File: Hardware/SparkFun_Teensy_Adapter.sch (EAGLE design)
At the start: 19 parts, among them U1 5V

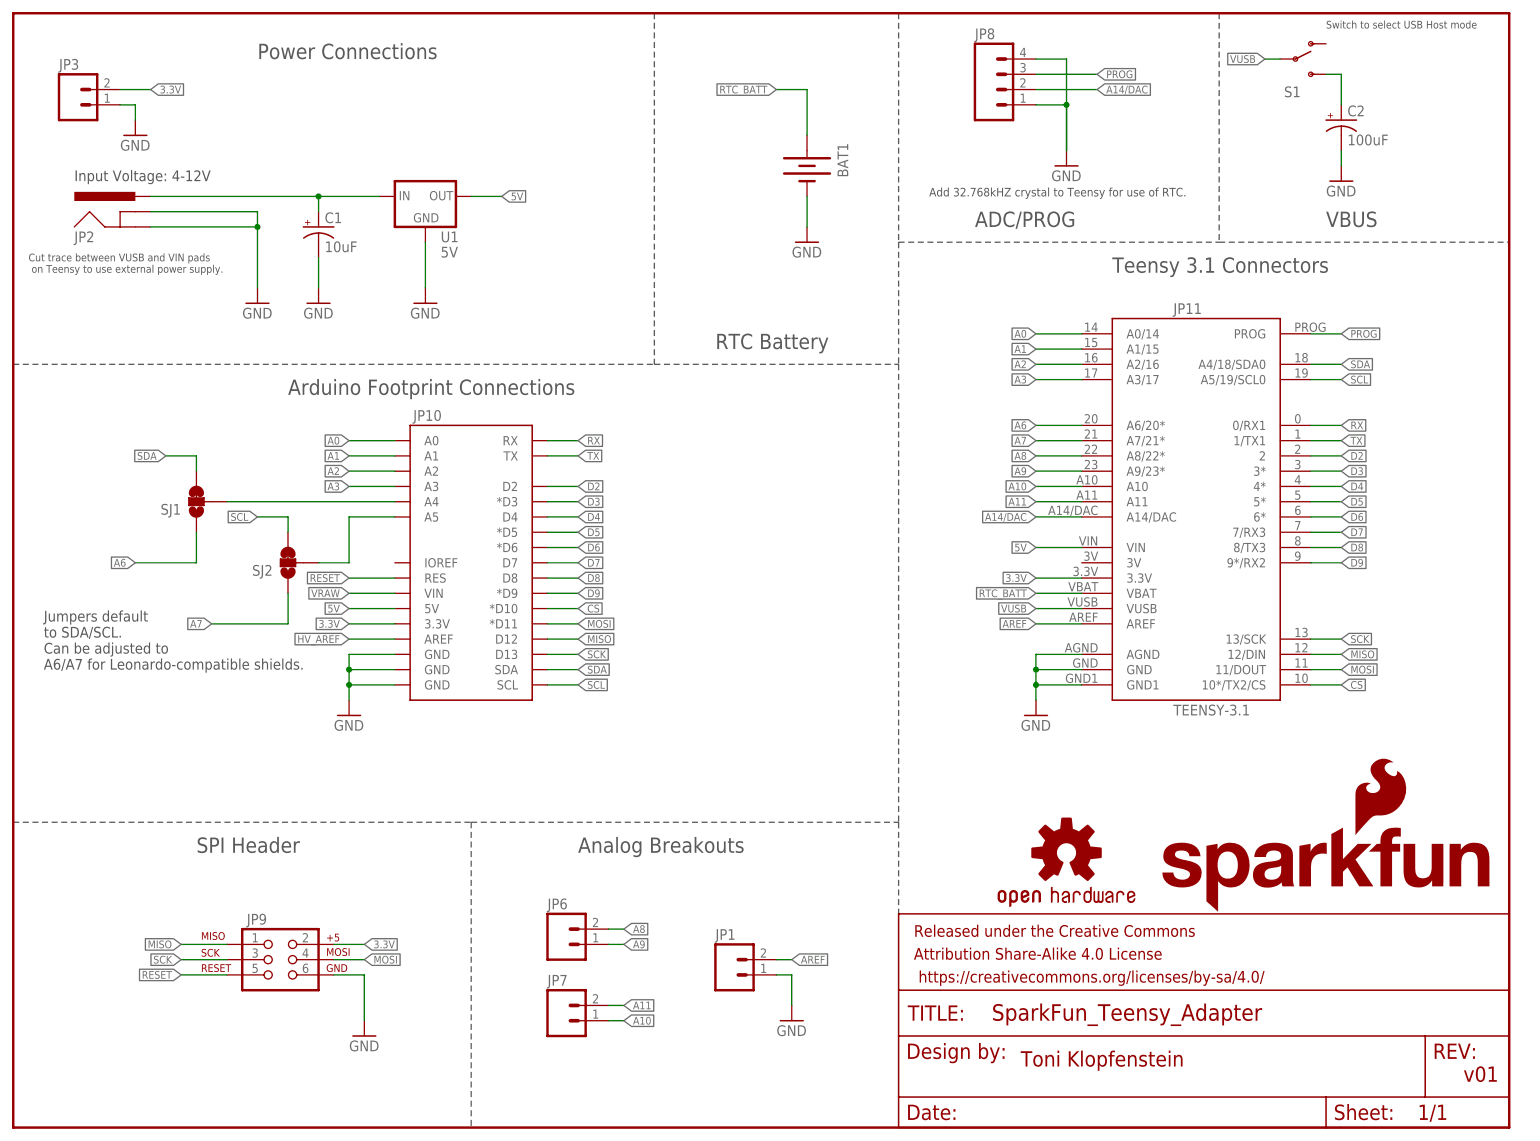
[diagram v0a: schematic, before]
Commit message: Moving vias from under regulator, removing USB host shield parts
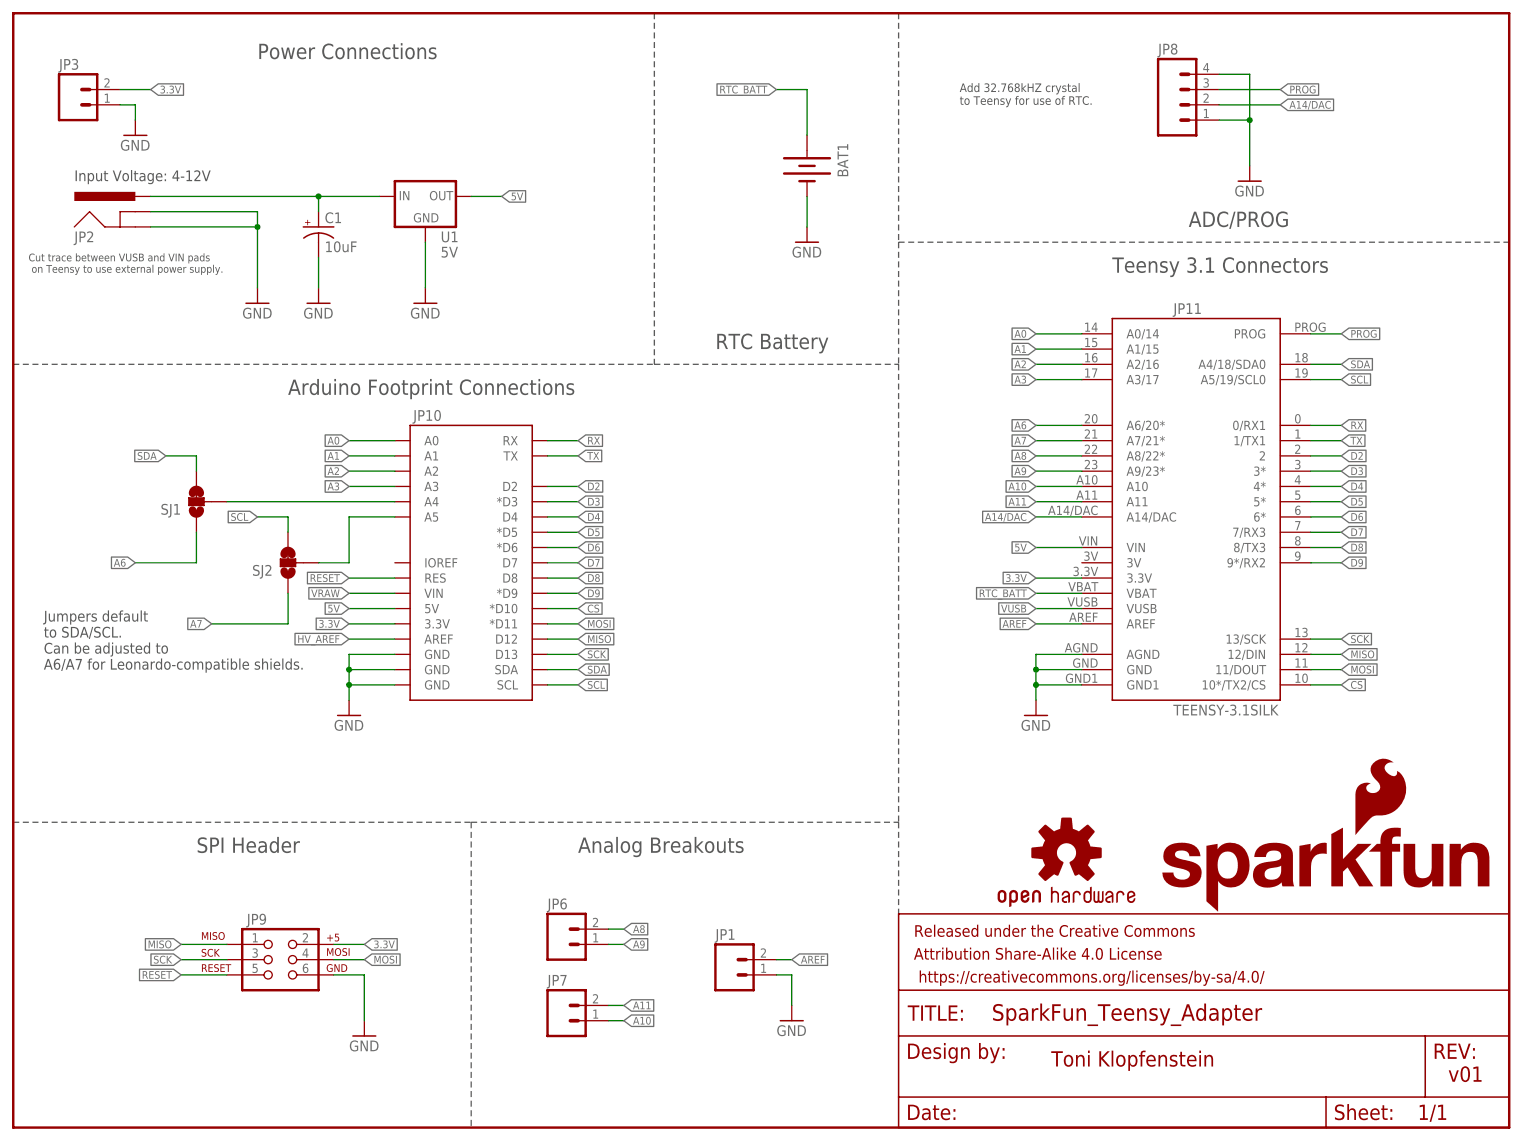
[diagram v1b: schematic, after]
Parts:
- removed C2: 100uF, SparkFun-Capacitors:100UF-25V-20%(PTH)
- removed S1: (no value), SparkFun-Electromechanical:SWITCH-SPDTPTH
- JP1, JP6, JP7: value M02PTH -> (none)
- JP11: value TEENSY-3.1 -> TEENSY-3.1SILK; device Testing:TEENSY-3.1 -> Testing:TEENSY-3.1SILK
- JP3: value M02JST-PTH-2 -> (none)
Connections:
- removed net N$1: C2.+, S1.S
- net GND: no longer C2.-
- net VUSB: no longer S1.P
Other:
- note removed: "Switch to select USB Host mode"
- note removed: "VBUS"
- moved on the sheet: JP8
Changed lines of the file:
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@@
 <layer number="56" name="wert" color="7" fill="1" visible="no" active="no"/>
 <layer number="57" name="tCAD" color="7" fill="1" visible="no" active="no"/>
+<layer number="59" name="tCarbon" color="7" fill="1" visible="no" active="no"/>
+<layer number="60" name="bCarbon" color="7" fill="1" visible="no" active="no"/>
 <layer number="90" name="Modules" color="5" fill="1" visible="yes" active="yes"/>
 <layer number="91" name="Nets" color="2" fill="1" visible="yes" active="yes"/>
@@
 <layer number="127" name="_tValues" color="7" fill="1" visible="yes" active="yes"/>
 <layer number="128" name="_bValues" color="7" fill="1" visible="yes" active="yes"/>
+<layer number="129" name="Mask" color="7" fill="1" visible="yes" active="yes"/>
 <layer number="131" name="tAdjust" color="7" fill="1" visible="yes" active="yes"/>
 <layer number="132" name="bAdjust" color="7" fill="1" visible="yes" active="yes"/>
@@
 <part name="JP10" library="Testing" deviceset="ARDUINO_R3_SHIELD" device="UNO_R3_SHIELD_HOLES"/>
 <part name="JP9" library="SparkFun-Connectors" deviceset="AVR_SPI_PRG_6" device="PTH"/>
-<part name="JP11" library="Testing" deviceset="TEENSY-3.1" device=""/>
+<part name="JP11" library="Testing" deviceset="TEENSY-3.1" device="SILK"/>
 <part name="GND1" library="SparkFun-Aesthetics" deviceset="GND" device=""/>
 <part name="GND2" library="SparkFun-Aesthetics" deviceset="GND" device=""/>
@@
 <part name="JP8" library="SparkFun-Connectors" deviceset="M04" device="PTH"/>
 <part name="GND9" library="SparkFun-Aesthetics" deviceset="GND" device=""/>
-<part name="GND11" library="SparkFun-Aesthetics" deviceset="GND" device=""/>
 <part name="BAT1" library="SparkFun-Electromechanical" deviceset="BATTERY" device="12PTH"/>
 <part name="GND4" library="SparkFun-Aesthetics" deviceset="GND" device=""/>
 <part name="JP1" library="SparkFun-Connectors" deviceset="M02" device="PTH"/>
 <part name="GND10" library="SparkFun-Aesthetics" deviceset="GND" device=""/>
-<part name="S1" library="SparkFun-Electromechanical" deviceset="SWITCH-SPDT" device="PTH"/>
 <part name="U1" library="SparkFun-PowerIC" deviceset="V_REG_78XX" device="-TO-220" value="5V"/>
-<part name="C2" library="SparkFun-Capacitors" deviceset="100UF-25V-20%(PTH)" device="" value="100uF"/>
 </parts>
 <sheets>
@@
 <plain>
 <text x="10.16" y="157.48" size="1.778" layer="97">Input Voltage: 4-12V</text>
-<text x="218.44" y="182.88" size="1.27" layer="97">Switch to select USB Host mode</text>
-<text x="152.4" y="154.94" size="1.4224" layer="97">Add 32.768kHZ crystal to Teensy for use of RTC.  </text>
+<text x="157.48" y="170.18" size="1.4224" layer="97">Add 32.768kHZ crystal
+to Teensy for use of RTC.  </text>
 <text x="2.54" y="142.24" size="1.27" layer="97">Cut trace between VUSB and VIN pads
  on Teensy to use external power supply. </text>
@@
 <wire x1="0" y1="127" x2="106.68" y2="127" width="0.2032" layer="97" style="shortdash"/>
 <wire x1="106.68" y1="127" x2="147.32" y2="127" width="0.2032" layer="97" style="shortdash"/>
-<wire x1="147.32" y1="147.32" x2="200.66" y2="147.32" width="0.2032" layer="97" style="shortdash"/>
-<wire x1="200.66" y1="147.32" x2="248.92" y2="147.32" width="0.2032" layer="97" style="shortdash"/>
+<wire x1="147.32" y1="147.32" x2="248.92" y2="147.32" width="0.2032" layer="97" style="shortdash"/>
 <wire x1="198.12" y1="185.42" x2="200.66" y2="185.42" width="0.2032" layer="97" style="shortdash"/>
-<wire x1="200.66" y1="185.42" x2="200.66" y2="147.32" width="0.2032" layer="97" style="shortdash"/>
 <text x="40.64" y="177.8" size="2.54" layer="97">Power Connections</text>
 <text x="45.72" y="121.92" size="2.54" layer="97">Arduino Footprint Connections</text>
@@
 <text x="93.98" y="45.72" size="2.54" layer="97">Analog Breakouts</text>
 <text x="182.88" y="142.24" size="2.54" layer="97">Teensy 3.1 Connectors</text>
-<text x="160.02" y="149.86" size="2.54" layer="97">ADC/PROG</text>
-<text x="218.44" y="149.86" size="2.54" layer="97">VBUS</text>
+<text x="195.58" y="149.86" size="2.54" layer="97">ADC/PROG</text>
 <wire x1="106.68" y1="185.42" x2="106.68" y2="127" width="0.2032" layer="97" style="shortdash"/>
 <text x="116.84" y="129.54" size="2.54" layer="97">RTC Battery</text>
-<text x="241.3" y="7.62" size="2.54" layer="94">v01</text>
-<text x="167.64" y="10.16" size="2.54" layer="94">Toni Klopfenstein</text>
+<text x="238.76" y="7.62" size="2.54" layer="94">v01</text>
+<text x="172.72" y="10.16" size="2.54" layer="94">Toni Klopfenstein</text>
 </plain>
 <instances>
@@
 <attribute name="NAME" x="88.9" y="23.622" size="1.778" layer="95"/>
 </instance>
-<instance part="JP8" gate="G$1" x="165.1" y="172.72"/>
-<instance part="GND9" gate="1" x="175.26" y="160.02"/>
-<instance part="GND11" gate="1" x="220.98" y="157.48"/>
+<instance part="JP8" gate="G$1" x="195.58" y="170.18"/>
+<instance part="GND9" gate="1" x="205.74" y="157.48"/>
 <instance part="BAT1" gate="G$1" x="132.08" y="160.02" rot="R270"/>
 <instance part="GND4" gate="1" x="132.08" y="147.32"/>
@@
 </instance>
 <instance part="GND10" gate="1" x="129.54" y="17.78"/>
-<instance part="S1" gate="1" x="213.36" y="177.8"/>
 <instance part="U1" gate="G$1" x="68.58" y="154.94"/>
-<instance part="C2" gate="G$1" x="220.98" y="167.64"/>
 </instances>
 <busses>
@@
 <segment>
 <pinref part="JP8" gate="G$1" pin="1"/>
-<wire x1="170.18" y1="170.18" x2="175.26" y2="170.18" width="0.1524" layer="91"/>
-<wire x1="175.26" y1="170.18" x2="175.26" y2="162.56" width="0.1524" layer="91"/>
+<wire x1="200.66" y1="167.64" x2="205.74" y2="167.64" width="0.1524" layer="91"/>
 <pinref part="GND9" gate="1" pin="GND"/>
 <pinref part="JP8" gate="G$1" pin="4"/>
-<wire x1="170.18" y1="177.8" x2="175.26" y2="177.8" width="0.1524" layer="91"/>
-<wire x1="175.26" y1="177.8" x2="175.26" y2="170.18" width="0.1524" layer="91"/>
-<junction x="175.26" y="170.18"/>
-<wire x1="175.26" y1="170.18" x2="175.26" y2="162.56" width="0.1524" layer="91"/>
+<wire x1="200.66" y1="175.26" x2="205.74" y2="175.26" width="0.1524" layer="91"/>
+<wire x1="205.74" y1="175.26" x2="205.74" y2="167.64" width="0.1524" layer="91"/>
+<junction x="205.74" y="167.64"/>
+<wire x1="205.74" y1="167.64" x2="205.74" y2="160.02" width="0.1524" layer="91"/>
 </segment>
 <segment>
@@
 <wire x1="129.54" y1="25.4" x2="129.54" y2="20.32" width="0.1524" layer="91"/>
 <pinref part="GND10" gate="1" pin="GND"/>
-</segment>
-<segment>
-<pinref part="GND11" gate="1" pin="GND"/>
-<wire x1="220.98" y1="162.56" x2="220.98" y2="160.02" width="0.1524" layer="91"/>
-<pinref part="C2" gate="G$1" pin="-"/>
 </segment>
 <segment>
@@
 <label x="170.18" y="86.36" size="1.27" layer="95" rot="R180" xref="yes"/>
 </segment>
-<segment>
-<pinref part="S1" gate="1" pin="P"/>
-<wire x1="210.82" y1="177.8" x2="208.28" y2="177.8" width="0.1524" layer="91"/>
-<label x="208.28" y="177.8" size="1.27" layer="95" rot="R180" xref="yes"/>
-</segment>
 </net>
 <net name="PROG" class="0">
@@
 <segment>
 <pinref part="JP8" gate="G$1" pin="3"/>
-<wire x1="170.18" y1="175.26" x2="180.34" y2="175.26" width="0.1524" layer="91"/>
-<label x="180.34" y="175.26" size="1.27" layer="95" xref="yes"/>
+<wire x1="200.66" y1="172.72" x2="210.82" y2="172.72" width="0.1524" layer="91"/>
+<label x="210.82" y="172.72" size="1.27" layer="95" xref="yes"/>
 </segment>
 </net>
@@
 <segment>
 <pinref part="JP8" gate="G$1" pin="2"/>
-<wire x1="170.18" y1="172.72" x2="180.34" y2="172.72" width="0.1524" layer="91"/>
-<label x="180.34" y="172.72" size="1.27" layer="95" xref="yes"/>
-</segment>
-</net>
-<net name="N$1" class="0">
-<segment>
-<pinref part="S1" gate="1" pin="S"/>
-<wire x1="218.44" y1="175.26" x2="220.98" y2="175.26" width="0.1524" layer="91"/>
-<wire x1="220.98" y1="175.26" x2="220.98" y2="170.18" width="0.1524" layer="91"/>
-<pinref part="C2" gate="G$1" pin="+"/>
-</segment>
-</net>
+<wire x1="200.66" y1="170.18" x2="210.82" y2="170.18" width="0.1524" layer="91"/>
+<label x="210.82" y="170.18" size="1.27" layer="95" xref="yes"/>
+</segment>
+</net>
